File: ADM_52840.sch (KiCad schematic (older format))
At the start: 41 parts, among them J1 JST, J3 Conn_01x16_Male, J4 Conn_01x19_Male, J5 JTAG, P1 USB_micro_B, Q1 DMP2045U, SW1 BTN1, SW2 BTN2, SW3 RESET, U1 HolyIOT_NRF52840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

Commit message: New Schematic
Optimisation for naming the pinout
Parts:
- removed D2: LED2, LEGACY:SM0603, symbol Device:LED
- removed R8: 330, LEGACY:SM0603, symbol Device:R
- J4: value Conn_01x19_Male -> Conn_01x20_Male; footprint Connector_PinHeader_2.54mm:PinHeader_1x19_P2.54mm_Vertical -> Connector_PinHeader_2.54mm:PinHeader_1x20_P2.54mm_Vertical; symbol Connector:Conn_01x19_Male -> Connector:Conn_01x20_Male
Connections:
- net GND: now also J4.20 (Pin_20); no longer J4.19 (Pin_19)
- net SK_SIGNAL: now also U1.22 (P0.26); no longer U1.10 (P0.30)
- net at J4.7 (Pin_7): now also U1.9 (P0.29); no longer U1.14 (P1.14)
- net at J4.8 (Pin_8): now also U1.10 (P0.30); no longer U1.15 (P1.12)
- net at J4.9 (Pin_9): now also U1.12 (P0.04); no longer U1.16 (P0.25)
- net at J4.10 (Pin_10): now also U1.13 (P0.05); no longer U1.17 (P0.11)
- net at J4.11 (Pin_11): now also U1.16 (P0.25); no longer U1.18 (P1.08)
- net at J4.12 (Pin_12): now also U1.17 (P0.11); no longer U1.19 (P0.27)
- net at U1.2 (P1.10): now also D1.2 (A); no longer J4.1 (Pin_1)
- net at J4.13 (Pin_13): now also U1.18 (P1.08); no longer U1.20 (P0.08)
- net at J4.14 (Pin_14): now also U1.19 (P0.27); no longer U1.21 (P0.06)
- net at J4.15 (Pin_15): now also U1.20 (P0.08); no longer U1.22 (P0.26)
- net at U1.3 (P1.11): now also J4.1 (Pin_1); no longer J4.2 (Pin_2)
- net at U1.4 (P1.13): now also J4.2 (Pin_2); no longer J4.3 (Pin_3)
- net at U1.5 (P1.15): now also J4.3 (Pin_3); no longer J4.4 (Pin_4)
- net at U1.52 (P0.12): now also J4.19 (Pin_19); no longer J4.18 (Pin_18)
- net at U1.53 (P1.09): now also J4.18 (Pin_18); no longer J4.17 (Pin_17)
- net at J4.16 (Pin_16): now also U1.21 (P0.06); no longer U1.54 (P0.07)
- net at U1.6 (P0.03): now also J4.4 (Pin_4); no longer J4.5 (Pin_5)
- net at U1.7 (P0.02): now also J4.5 (Pin_5); no longer J4.6 (Pin_6)
- net at U1.8 (P0.28): now also J4.6 (Pin_6); no longer D1.2 (A)
- net P0.04 renamed P1.14
- net P1.14: now also U1.14 (P1.14); no longer U1.12 (P0.04)
- net P0.05 renamed P1.12
- net P1.12: now also U1.15 (P1.12); no longer U1.13 (P0.05)
- new net: J4.17 (Pin_17), U1.54 (P0.07)
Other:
- moved on the sheet: D1, R7
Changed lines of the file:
@@
 L Device:LED D1
 U 1 1 5F9E33A5
-P 1575 1500
-F 0 "D1" H 1700 1450 50  0000 C CNN
-F 1 "LED1" H 1475 1350 50  0000 C CNN
-F 2 "LEGACY:SM0603" H 1575 1500 50  0001 C CNN
-F 3 "~" H 1575 1500 50  0001 C CNN
-	1    1575 1500
+P 2000 775
+F 0 "D1" H 2200 850 50  0000 C CNN
+F 1 "LED1" H 2000 900 50  0000 C CNN
+F 2 "LEGACY:SM0603" H 2000 775 50  0001 C CNN
+F 3 "~" H 2000 775 50  0001 C CNN
+	1    2000 775
 	1    0    0    -1
 $EndComp
@@
 	10250 1475 10425 1475
 $Comp
-L Device:LED D2
-U 1 1 5F9E299B
-P 1925 1600
-F 0 "D2" H 2050 1550 50  0000 C CNN
-F 1 "LED2" H 1875 1450 50  0000 C CNN
-F 2 "LEGACY:SM0603" H 1925 1600 50  0001 C CNN
-F 3 "~" H 1925 1600 50  0001 C CNN
-	1    1925 1600
-	1    0    0    -1
-$EndComp
-$Comp
 L power:GND #PWR08
 U 1 1 5FCD9296
-P 1500 1900
-F 0 "#PWR08" H 1500 1650 50  0001 C CNN
-F 1 "GND" H 1350 1825 50  0000 C CNN
-F 2 "" H 1500 1900 50  0001 C CNN
-F 3 "" H 1500 1900 50  0001 C CNN
-	1    1500 1900
+P 750 800
+F 0 "#PWR08" H 750 550 50  0001 C CNN
+F 1 "GND" H 600 725 50  0000 C CNN
+F 2 "" H 750 800 50  0001 C CNN
+F 3 "" H 750 800 50  0001 C CNN
+	1    750  800
 	1    0    0    -1
 $EndComp
@@
 Text Notes 1050 7700 0    118  ~ 0
 SK6812
-Text GLabel 2850 1700 0    50   Input ~ 0
+Text GLabel 3300 2900 0    50   Input ~ 0
 SK_SIGNAL
 Text GLabel 1950 6800 2    50   Input ~ 0
@@
 	3000 800  3700 800
 Wire Wire Line
-	2450 900  3700 900
-Wire Wire Line
 	5250 3200 5250 3500
 Wire Wire Line
@@
 	6625 1825 6625 1800
 $Comp
-L Connector:Conn_01x19_Male J4
+L Connector:Conn_01x20_Male J4
 U 1 1 5FBCF5CF
-P 1925 3950
-F 0 "J4" V 1852 3878 50  0000 C CNN
-F 1 "Conn_01x19_Male" V 1761 3878 50  0001 C CNN
-F 2 "Connector_PinHeader_2.54mm:PinHeader_1x19_P2.54mm_Vertical" H 1925 3950 50  0001 C CNN
-F 3 "~" H 1925 3950 50  0001 C CNN
-	1    1925 3950
+P 1825 3950
+F 0 "J4" V 1752 3878 50  0000 C CNN
+F 1 "Conn_01x20_Male" V 1661 3878 50  0001 C CNN
+F 2 "Connector_PinHeader_2.54mm:PinHeader_1x20_P2.54mm_Vertical" H 1825 3950 50  0001 C CNN
+F 3 "~" H 1825 3950 50  0001 C CNN
+	1    1825 3950
 	0    -1   -1   0
 $EndComp
-Wire Wire Line
-	2650 1000 2650 925
-Wire Wire Line
-	2650 925  800  925
-Wire Wire Line
-	800  925  800  3500
-Wire Wire Line
-	2650 1000 3700 1000
-Wire Wire Line
-	2450 900  2450 850
-Wire Wire Line
-	2450 850  725  850
-Wire Wire Line
-	725  850  725  3550
 Wire Wire Line
 	4350 4075 3475 4075
@@
 L Device:R R7
 U 1 1 600A9D2C
-P 1300 1650
-F 0 "R7" H 1225 1500 50  0000 C CNN
-F 1 "330" V 1300 1650 50  0000 C CNN
-F 2 "LEGACY:SM0603" V 1230 1650 50  0001 C CNN
-F 3 "~" H 1300 1650 50  0001 C CNN
-	1    1300 1650
-	-1   0    0    -1
-$EndComp
-Wire Wire Line
-	1300 1500 1425 1500
-$Comp
-L Device:R R8
-U 1 1 6011CAE0
-P 1675 1750
-F 0 "R8" H 1575 1650 50  0000 C CNN
-F 1 "330" V 1675 1750 50  0000 C CNN
-F 2 "LEGACY:SM0603" V 1605 1750 50  0001 C CNN
-F 3 "~" H 1675 1750 50  0001 C CNN
-	1    1675 1750
-	-1   0    0    -1
-$EndComp
-Wire Wire Line
-	1300 1800 1300 1875
-Wire Wire Line
-	1300 1875 1500 1875
-Wire Wire Line
-	1500 1875 1500 1900
-Wire Wire Line
-	1500 1875 1600 1875
-Wire Wire Line
-	1600 1875 1600 1925
-Wire Wire Line
-	1600 1925 1675 1925
-Wire Wire Line
-	1675 1925 1675 1900
-Connection ~ 1500 1875
-Wire Wire Line
-	875  1100 3700 1100
-Wire Wire Line
-	3700 1200 950  1200
+P 1425 775
+F 0 "R7" V 1525 775 50  0000 C CNN
+F 1 "330" V 1425 775 50  0000 C CNN
+F 2 "LEGACY:SM0603" V 1355 775 50  0001 C CNN
+F 3 "~" H 1425 775 50  0001 C CNN
+	1    1425 775
+	0    1    -1   0
+$EndComp
 Wire Wire Line
 	3700 1800 3500 1800
 Wire Wire Line
-	3700 2200 1725 2200
-Wire Wire Line
-	1725 2200 1725 3750
-Wire Wire Line
-	3700 2100 2700 2100
-Wire Wire Line
-	2700 2100 2700 2150
-Wire Wire Line
-	2700 2150 1625 2150
-Wire Wire Line
-	1625 2150 1625 3750
-Wire Wire Line
-	1100 1400 1100 2275
-Wire Wire Line
-	1100 1400 3700 1400
-Wire Wire Line
-	1050 1300 3700 1300
-Wire Wire Line
-	1125 3500 1125 3750
-Wire Wire Line
-	800  3500 1125 3500
-Wire Wire Line
-	1025 3750 1025 3550
-Wire Wire Line
-	725  3550 1025 3550
-Wire Wire Line
-	875  3400 1225 3400
-Wire Wire Line
-	1225 3400 1225 3750
-Wire Wire Line
-	875  1100 875  3400
-Wire Wire Line
-	950  3300 1325 3300
-Wire Wire Line
-	1325 3300 1325 3750
-Wire Wire Line
-	950  1200 950  3300
-Wire Wire Line
-	1050 1300 1050 3200
-Wire Wire Line
-	1050 3200 1425 3200
-Wire Wire Line
-	1425 3200 1425 3750
-Wire Wire Line
-	1525 2275 1525 3750
-Wire Wire Line
-	1100 2275 1525 2275
-Wire Wire Line
 	7550 2900 7550 2525
 Wire Wire Line
@@
 Wire Wire Line
 	5850 2900 7550 2900
-Wire Wire Line
-	2850 1700 3700 1700
-Wire Wire Line
-	1725 1500 3700 1500
-Wire Wire Line
-	2075 1600 3700 1600
-Wire Wire Line
-	1775 1600 1675 1600
 Wire Wire Line
 	7625 2625 7600 2625
@@
 Text GLabel 7200 3050 0    50   Input ~ 0
 V_NRF
-Wire Wire Line
-	1825 2300 3700 2300
-Wire Wire Line
-	1825 2300 1825 3750
-Wire Wire Line
-	1925 2400 3700 2400
-Wire Wire Line
-	1925 2400 1925 3750
-Wire Wire Line
-	2025 2500 3700 2500
-Wire Wire Line
-	2025 2500 2025 3750
-Wire Wire Line
-	2125 2600 3700 2600
-Wire Wire Line
-	2125 2600 2125 3750
-Wire Wire Line
-	2225 2700 3700 2700
-Wire Wire Line
-	2225 2700 2225 3750
-Wire Wire Line
-	2325 2800 3700 2800
-Wire Wire Line
-	2325 2800 2325 3750
-Wire Wire Line
-	2425 2900 3700 2900
-Wire Wire Line
-	2425 2900 2425 3750
 Wire Wire Line
 	2825 3750 2825 3425
@@
 Wire Wire Line
 	4950 3850 5525 3850
-Text GLabel 3500 1900 0    50   Input ~ 0
-P0.04
-Text GLabel 3500 2000 0    50   Input ~ 0
-P0.05
-Wire Wire Line
-	3700 1900 3500 1900
-Wire Wire Line
-	3500 2000 3700 2000
+Text GLabel 3400 2100 0    50   Input ~ 0
+P1.14
+Text GLabel 3400 2200 0    50   Input ~ 0
+P1.12
 Text GLabel 4675 5525 2    50   Input ~ 0
-P0.04
+P1.14
 Text GLabel 6150 5525 2    50   Input ~ 0
-P0.05
+P1.12
 $Comp
 L Device:R R10
@@
 Wire Wire Line
 	2025 6950 2025 7275
+Wire Wire Line
+	1275 775  750  775
+Wire Wire Line
+	750  775  750  800
+Wire Wire Line
+	1575 775  1850 775
+Wire Wire Line
+	2150 775  2725 775
+Wire Wire Line
+	2725 775  2725 900
+Wire Wire Line
+	2725 900  3700 900
+Wire Wire Line
+	3400 2100 3700 2100
+Wire Wire Line
+	3700 2200 3400 2200
+Wire Wire Line
+	3300 2900 3700 2900
+Wire Wire Line
+	3700 2800 2425 2800
+Wire Wire Line
+	2425 2800 2425 3750
+Wire Wire Line
+	3700 2700 2325 2700
+Wire Wire Line
+	2325 2700 2325 3750
+Wire Wire Line
+	3700 2600 2225 2600
+Wire Wire Line
+	2225 2600 2225 3750
+Wire Wire Line
+	3700 2500 2125 2500
+Wire Wire Line
+	2125 2500 2125 3750
+Wire Wire Line
+	3700 2400 2025 2400
+Wire Wire Line
+	2025 2400 2025 3750
+Wire Wire Line
+	3700 2300 1925 2300
+Wire Wire Line
+	1925 2300 1925 3750
+Wire Wire Line
+	3700 2000 1825 2000
+Wire Wire Line
+	1825 2000 1825 3750
+Wire Wire Line
+	3700 1900 1725 1900
+Wire Wire Line
+	1725 1900 1725 3750
+Wire Wire Line
+	3700 1700 1625 1700
+Wire Wire Line
+	1625 1700 1625 3750
+Wire Wire Line
+	3700 1600 1525 1600
+Wire Wire Line
+	1525 1600 1525 3750
+Wire Wire Line
+	3700 1500 1425 1500
+Wire Wire Line
+	1425 1500 1425 3750
+Wire Wire Line
+	3700 1400 1325 1400
+Wire Wire Line
+	1325 1400 1325 3750
+Wire Wire Line
+	3700 1300 1225 1300
+Wire Wire Line
+	1225 1300 1225 3750
+Wire Wire Line
+	3700 1200 1125 1200
+Wire Wire Line
+	1125 1200 1125 3750
+Wire Wire Line
+	3700 1100 1025 1100
+Wire Wire Line
+	1025 1100 1025 3750
+Wire Wire Line
+	3700 1000 925  1000
+Wire Wire Line
+	925  1000 925  3750
 $EndSCHEMATC

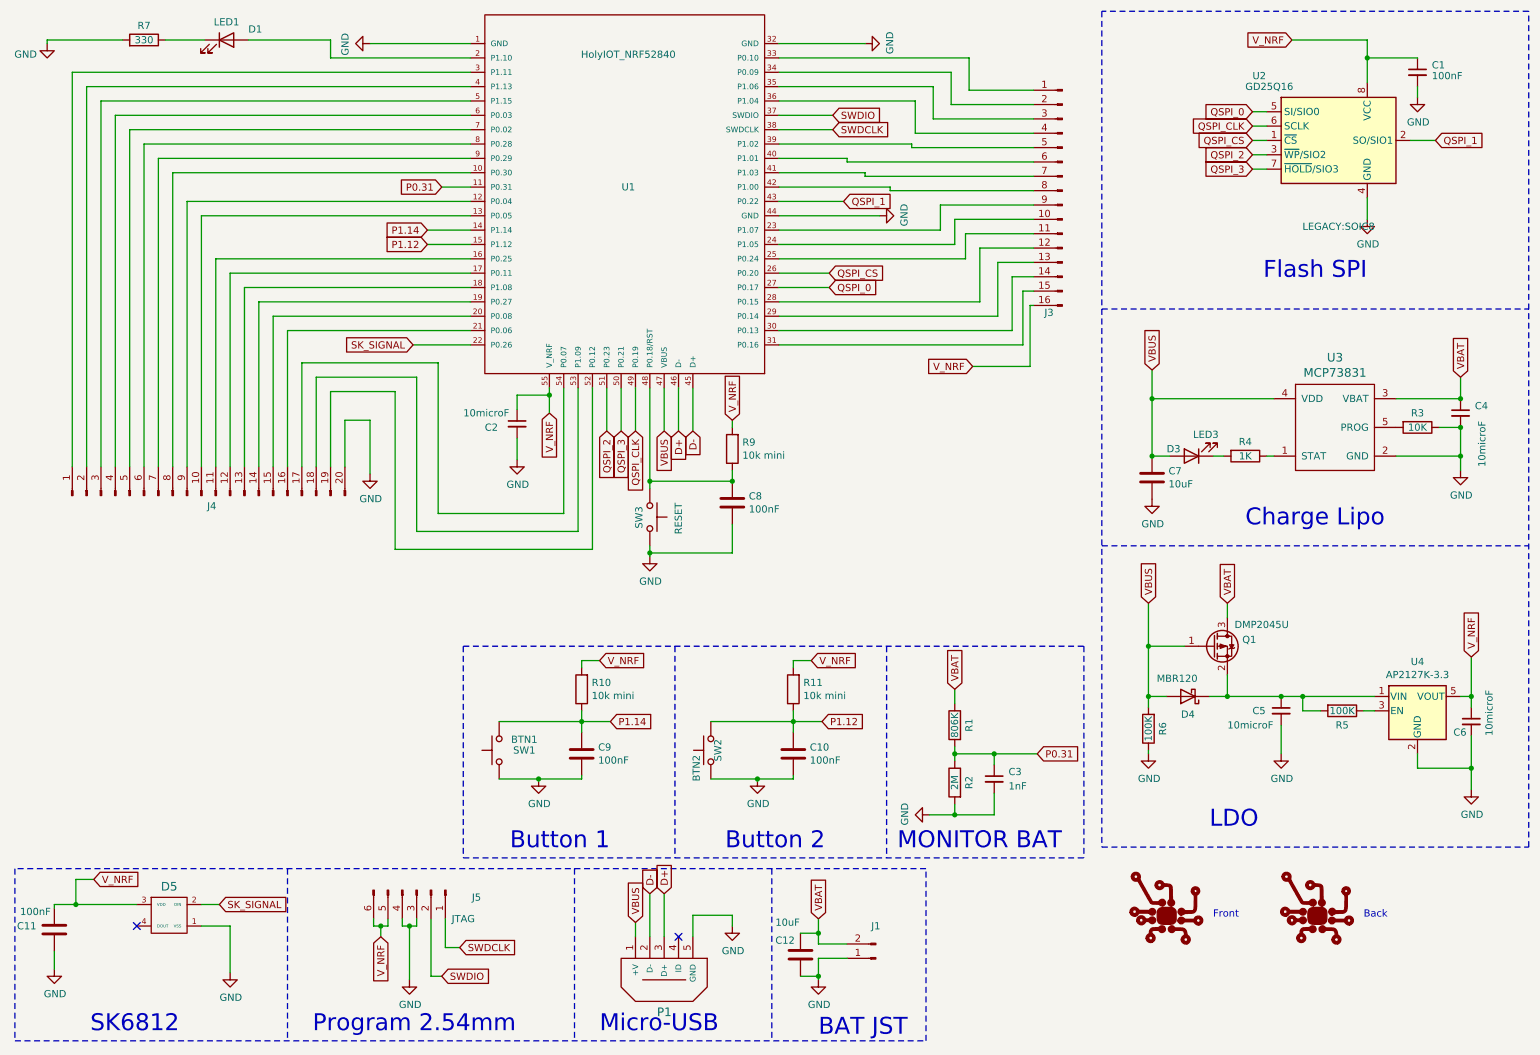
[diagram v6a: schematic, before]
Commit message: Routing
Made new revision with good pinout for routing
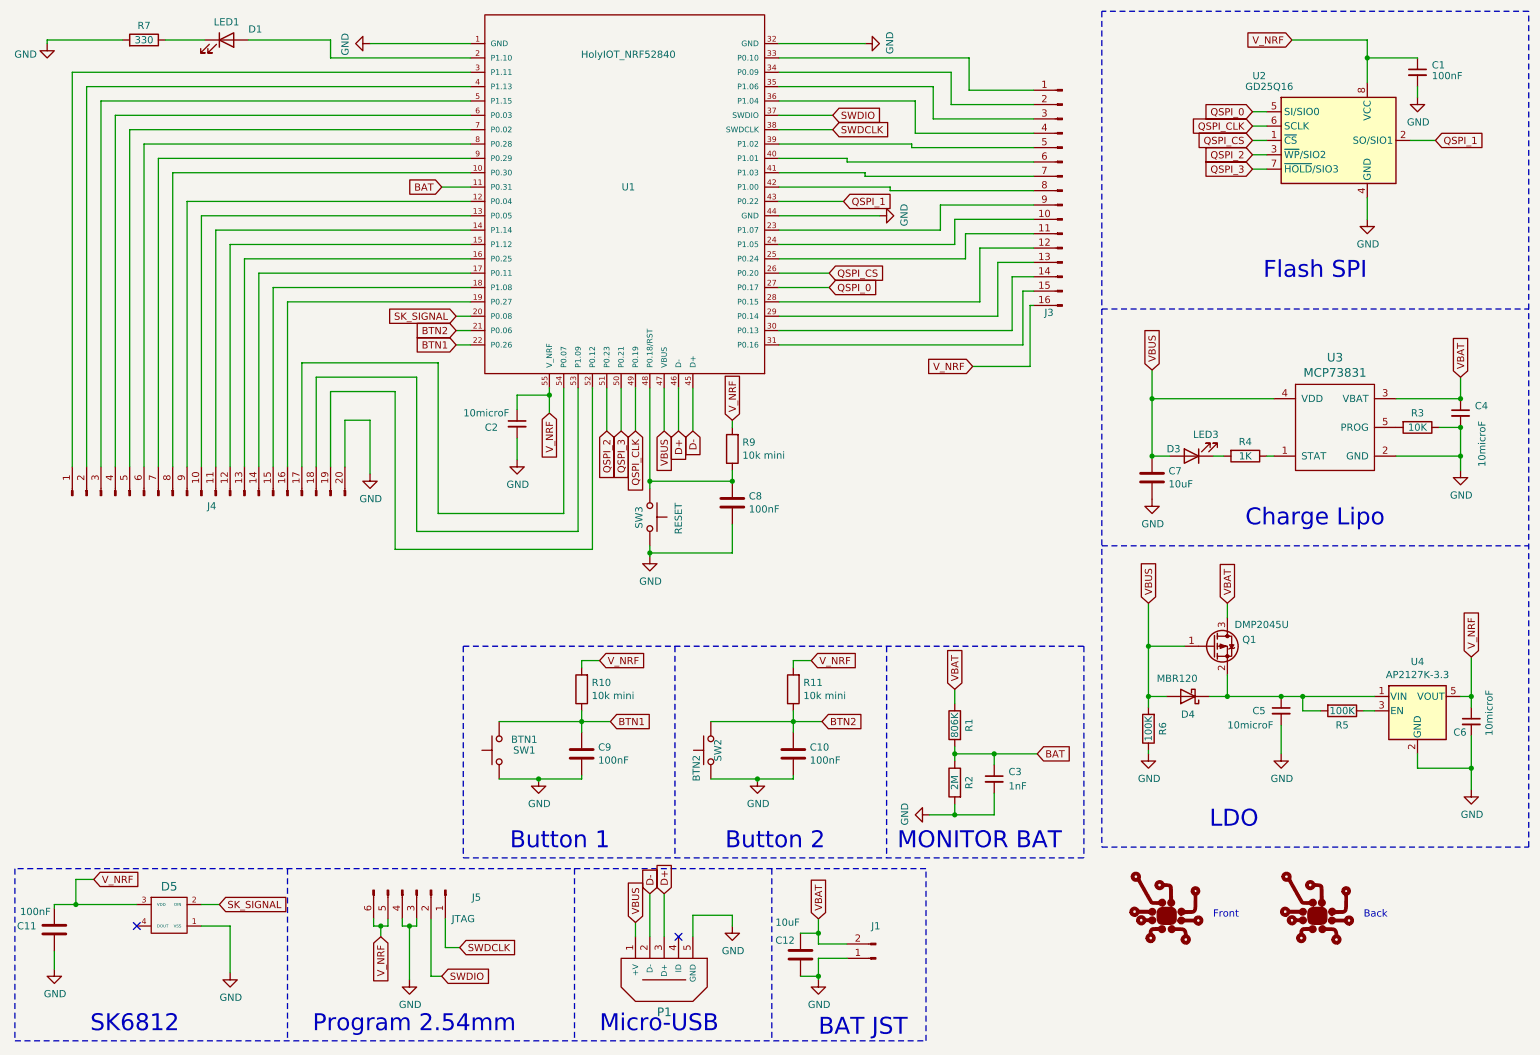
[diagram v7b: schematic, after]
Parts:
- added G1: LOGO, LEGACY:adm_lite, symbol ADM_52840-rescue:LOGO-seri
- added G2: LOGO, LEGACY:adm, symbol ADM_52840-rescue:LOGO-seri
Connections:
- net SK_SIGNAL: now also U1.20 (P0.08); no longer U1.22 (P0.26)
- net at J4.11 (Pin_11): now also U1.14 (P1.14); no longer U1.16 (P0.25)
- net at J4.12 (Pin_12): now also U1.15 (P1.12); no longer U1.17 (P0.11)
- net at J4.13 (Pin_13): now also U1.16 (P0.25); no longer U1.18 (P1.08)
- net at J4.14 (Pin_14): now also U1.17 (P0.11); no longer U1.19 (P0.27)
- net at J4.15 (Pin_15): now also U1.18 (P1.08); no longer U1.20 (P0.08)
- net at J4.16 (Pin_16): now also U1.19 (P0.27); no longer U1.21 (P0.06)
- net P0.31 renamed BAT
- net P1.12 renamed BTN2
- net BTN2: now also U1.21 (P0.06); no longer U1.15 (P1.12)
- net P1.14 renamed BTN1
- net BTN1: now also U1.22 (P0.26); no longer U1.14 (P1.14)
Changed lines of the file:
@@
 F 0 "U2" H 9150 1925 50  0000 L CNN
 F 1 "GD25Q16" H 9100 1850 50  0000 L CNN
-F 2 "LEGACY:SOIC8" H 9750 875 50  0000 C CNN
+F 2 "LEGACY:SOIC8" H 9750 875 50  0001 C CNN
 F 3 "" H 9750 1475 50  0001 C CNN
 	1    9750 1475
@@
 Text Notes 1050 7700 0    118  ~ 0
 SK6812
-Text GLabel 3300 2900 0    50   Input ~ 0
+Text GLabel 3600 2700 0    50   Input ~ 0
 SK_SIGNAL
 Text GLabel 1950 6800 2    50   Input ~ 0
@@
 VBAT
 Text GLabel 3500 1800 0    50   Input ~ 0
-P0.31
+BAT
 Wire Wire Line
 	7350 5750 7650 5750
 Text GLabel 7650 5750 2    50   Input ~ 0
-P0.31
+BAT
 Connection ~ 7350 5750
 Text Notes 6675 6425 0    118  ~ 0
@@
 Wire Wire Line
 	4950 3850 5525 3850
-Text GLabel 3400 2100 0    50   Input ~ 0
-P1.14
-Text GLabel 3400 2200 0    50   Input ~ 0
-P1.12
-Text GLabel 4675 5525 2    50   Input ~ 0
-P1.14
-Text GLabel 6150 5525 2    50   Input ~ 0
-P1.12
+Text GLabel 3600 2800 0    50   Input ~ 0
+BTN2
+Text GLabel 3600 2900 0    50   Input ~ 0
+BTN1
 $Comp
 L Device:R R10
@@
 	3650 5000 7975 5000
 $Comp
-L ADM_52840-rescue:LOGO-seri #G1
+L ADM_52840-rescue:LOGO-seri G1
 U 1 1 5FA34F44
 P 8550 6825
-F 0 "#G1" H 8550 6606 60  0001 C CNN
+F 0 "G1" H 8550 6606 60  0001 C CNN
 F 1 "LOGO" H 8550 7044 60  0001 C CNN
 F 2 "LEGACY:adm_lite" H 8550 6825 50  0001 C CNN
@@
 $EndComp
 $Comp
-L ADM_52840-rescue:LOGO-seri #G2
+L ADM_52840-rescue:LOGO-seri G2
 U 1 1 5FA358D5
 P 9600 6825
-F 0 "#G2" H 9600 6606 60  0001 C CNN
+F 0 "G2" H 9600 6606 60  0001 C CNN
 F 1 "LOGO" H 9600 7044 60  0001 C CNN
 F 2 "LEGACY:adm" H 9600 6825 50  0001 C CNN
@@
 	2725 900  3700 900
 Wire Wire Line
-	3400 2100 3700 2100
-Wire Wire Line
-	3700 2200 3400 2200
-Wire Wire Line
-	3300 2900 3700 2900
-Wire Wire Line
-	3700 2800 2425 2800
-Wire Wire Line
-	2425 2800 2425 3750
-Wire Wire Line
-	3700 2700 2325 2700
-Wire Wire Line
-	2325 2700 2325 3750
-Wire Wire Line
-	3700 2600 2225 2600
-Wire Wire Line
-	2225 2600 2225 3750
-Wire Wire Line
-	3700 2500 2125 2500
-Wire Wire Line
-	2125 2500 2125 3750
-Wire Wire Line
-	3700 2400 2025 2400
-Wire Wire Line
-	2025 2400 2025 3750
-Wire Wire Line
-	3700 2300 1925 2300
-Wire Wire Line
-	1925 2300 1925 3750
+	3600 2900 3700 2900
 Wire Wire Line
 	3700 2000 1825 2000
@@
 Wire Wire Line
 	925  1000 925  3750
+Wire Wire Line
+	3700 2700 3600 2700
+Wire Wire Line
+	3600 2800 3700 2800
+Wire Wire Line
+	3700 2100 1925 2100
+Wire Wire Line
+	1925 2100 1925 3750
+Wire Wire Line
+	3700 2200 2025 2200
+Wire Wire Line
+	2025 2200 2025 3750
+Wire Wire Line
+	3700 2300 2125 2300
+Wire Wire Line
+	2125 2300 2125 3750
+Wire Wire Line
+	3700 2400 2225 2400
+Wire Wire Line
+	2225 2400 2225 3750
+Wire Wire Line
+	3700 2500 2325 2500
+Wire Wire Line
+	2325 2500 2325 3750
+Wire Wire Line
+	3700 2600 2425 2600
+Wire Wire Line
+	2425 2600 2425 3750
+Text GLabel 6150 5525 2    50   Input ~ 0
+BTN2
+Text GLabel 4675 5525 2    50   Input ~ 0
+BTN1
 $EndSCHEMATC
